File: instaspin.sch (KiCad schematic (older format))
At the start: 9 parts, among them J1 CONN_01X08, J2 CONN_01X12, J3 TMDSCNCD28069, J4 CONN_01X03, Q1 FDG1024NZ

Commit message: progress on V2 schematic
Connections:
- net labels added: TEMP_EN, TEMP_PWM, ~IFB_A
- net labels removed: IFB_A, IFB_BUS, MOTOR_TEMP, PWR_STG_TEMP, ~FLT_OTP
- wire segments 84 -> 81
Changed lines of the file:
@@
 VFB_BUS
 Text HLabel 5000 2450 2    60   Input ~ 0
-IFB_A
+~IFB_A
 Text HLabel 5000 2650 2    60   Input ~ 0
 IFB_B
 Text HLabel 5000 2850 2    60   Input ~ 0
 IFB_C
-Text HLabel 2400 1650 0    60   Input ~ 0
-PWR_STG_TEMP
-Text HLabel 2400 1850 0    60   Input ~ 0
-MOTOR_TEMP
-Text HLabel 5000 3050 2    60   Input ~ 0
-IFB_BUS
+Text HLabel 7000 1500 0    60   Input ~ 0
+TEMP_PWM
+Text HLabel 7000 1700 0    60   Output ~ 0
+TEMP_EN
 Text HLabel 2700 3250 0    60   Output ~ 0
 PWM_AH
@@
 Text HLabel 4950 4050 2    60   Input ~ 0
 ~FLT_DESAT
-Text HLabel 2550 4050 0    60   Input ~ 0
-~FLT_OTP
 Text HLabel 4950 4250 2    60   Input ~ 0
 PWR_RDY
@@
 	1950 2250 2700 2250
 Wire Wire Line
-	2400 1850 2700 1850
-Wire Wire Line
-	2400 1650 2700 1650
-Wire Wire Line
 	2400 2650 2700 2650
 Wire Wire Line
@@
 	5000 2850 4700 2850
 Wire Wire Line
-	4700 3050 5000 3050
-Wire Wire Line
 	2400 2450 2700 2450

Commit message: more v2 progress
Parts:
- added C? (x8): 2.2uF 10V, symbol C_Small
- added C? (x6): 2.2uF 6V, symbol C_Small
- added C? (x2): ? pF, symbol C_Small
- added C?: 0.1 uF, symbol C_Small
- added C?: 0.1uF 10V, symbol C_Small
- added P?: CONN_02X05, symbol CONN_02X05
- added P?: CONN_01X02, symbol CONN_01X02
- added R? (x4): 4.7k, symbol R_Small
- added R?: 170, symbol R_Small
- added R?: 330, symbol R_Small
- added U?: TMS320F28069M, MODULE, symbol TMS320F28069M
- added U?: ACPL-M61L, Housings_SOIC:SOIC-6_4.58x6.81mm_Pitch1.27mm, symbol ACPL-M61L
- added Y?: Crystal_Small, symbol Crystal_Small
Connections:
- net labels added: +1.8V, +3.3V, +3.3VA, +5VA, GPIO34, SYNCIO, TCK, TDI, TDO, TMS, ~DSP_RESET, ~TRST
- wire segments 81 -> 169
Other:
- note added: "Boot mode and JTAG"
- note added: "CAN"
- note added: "On transmitter, hand-pop LED resistors"
- moved on the sheet: D1, J1, J2, J3, J4, Q1A, Q1B, R1, W1, W2

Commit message: further V2 progress
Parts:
- added C? (x4): 0.1 uF, symbol C_Small
- added P?: CONN_01X03, symbol CONN_01X03
- added R? (x2): 1k, symbol R_Small
- added R?: 10k, symbol R_Small
- added R?: 33k, symbol R_Small
- added R?: 17k, symbol R_Small
- added R?: 330, symbol R_Small
- added U?: ADM3053, Housings_SOIC:SOIC-20_7.5x12.8mm_Pitch1.27mm, symbol ADM3053
- added W? (x7): TEST_1P, Measurement_Points:Measurement_Point_Round-SMD-Pad_Small, symbol TEST_1P
- R?: value 170 -> 170 0.5%
- R?: value 330 -> 330 0.5%
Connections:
- net labels added: CAN_RX, CAN_TX, LED1, LED2, SW_BRAKE, SW_EMERG, SW_FLIGHT, THRUST_PWM
- wire segments 169 -> 175
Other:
- note added: "Perhaps use resonator\nor SiTime?"
- moved on the sheet: J1

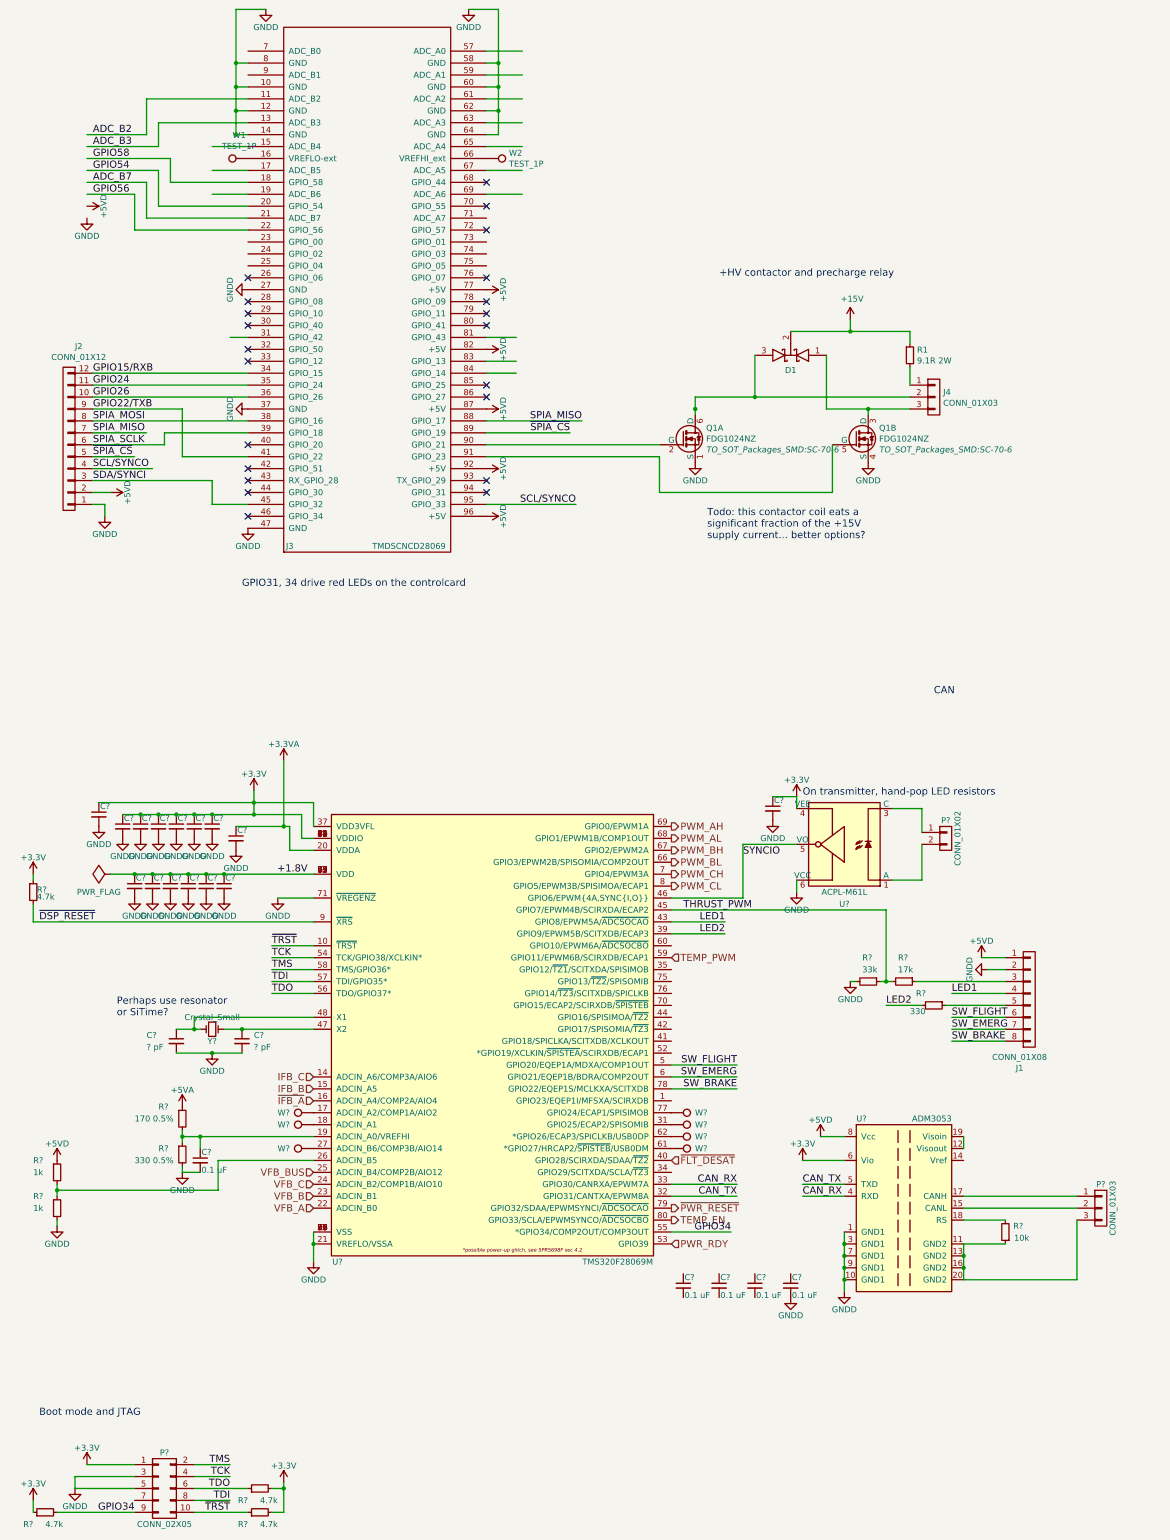
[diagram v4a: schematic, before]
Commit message: V2 schem complete, footprints not assigned
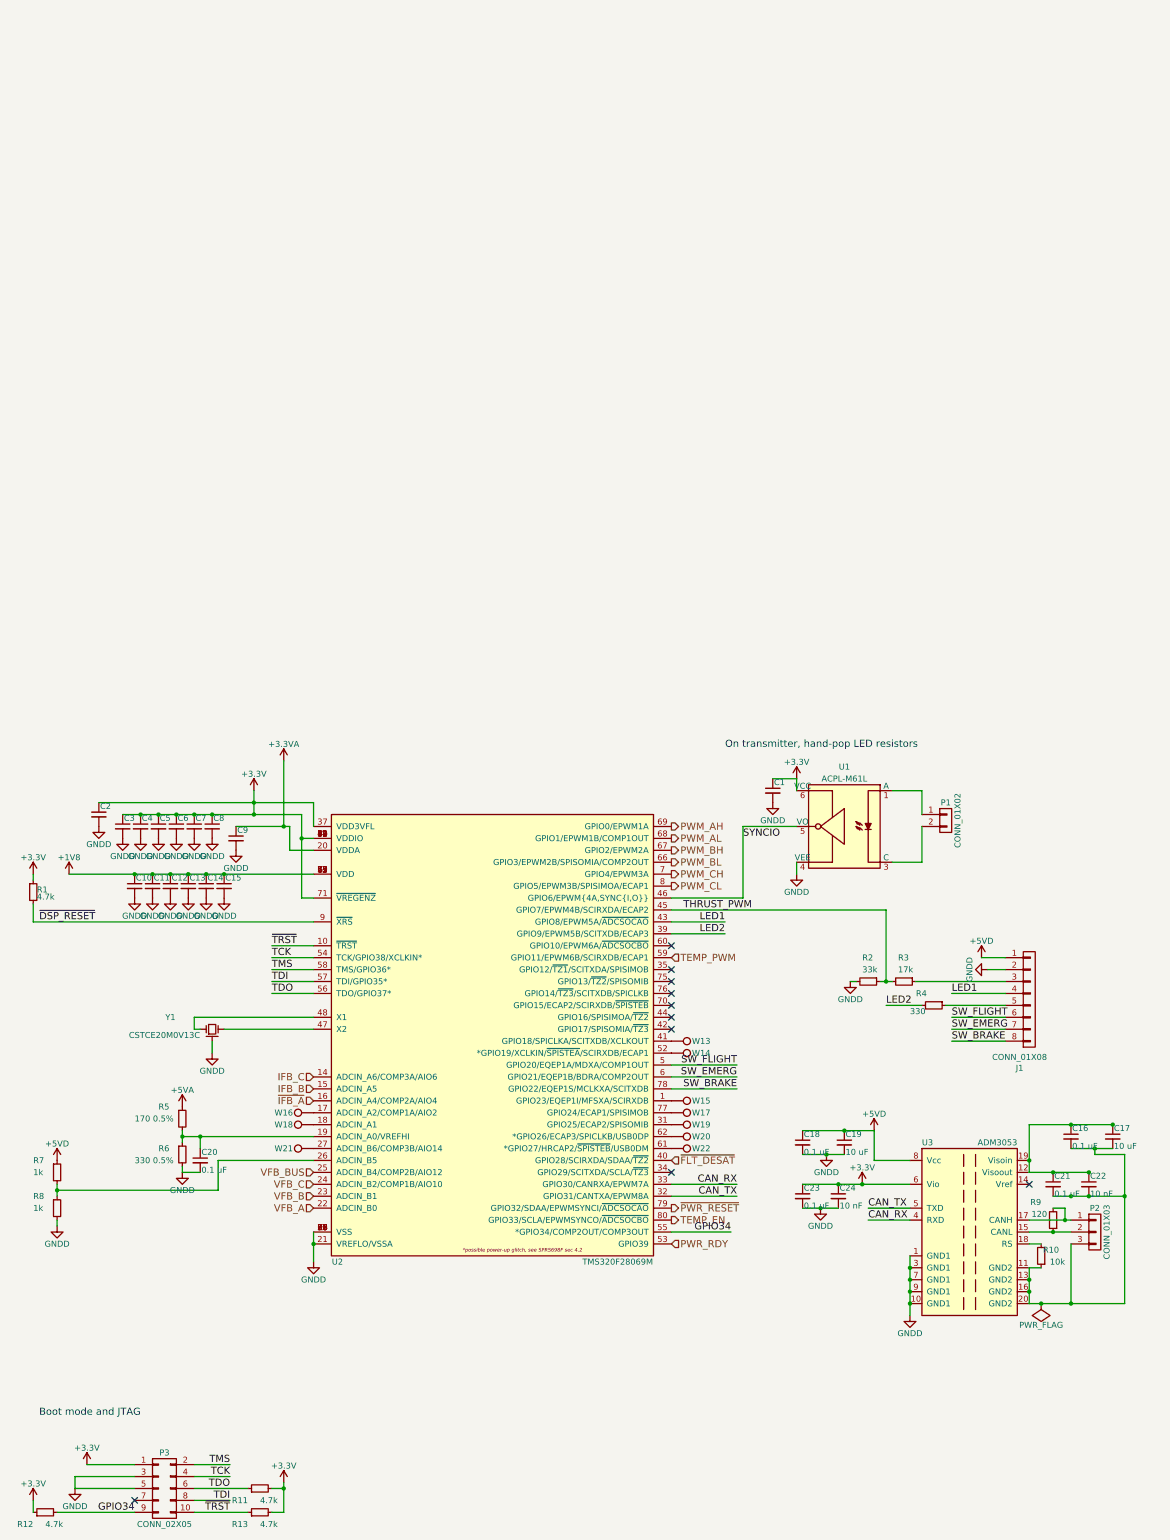
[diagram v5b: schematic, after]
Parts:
- removed C? (x2): ? pF, symbol C_Small
- removed D1: D_Schottky_x2_KCom_AKA, TO_SOT_Packages_SMD:SOT-323, symbol D_Schottky_x2_KCom_AKA
- removed J2: CONN_01X12, Connectors_Molex:Connector_Molex_PicoBlade_53261-1271, symbol CONN_01X12
- removed J3: TMDSCNCD28069, sictroller:5390213-1, symbol TMDSCNCD28069
- removed J4: CONN_01X03, sictroller:Molex-SL-3POS-RA, symbol CONN_01X03
- removed Q1: FDG1024NZ, TO_SOT_Packages_SMD:SC-70-6, symbol FDG1024NZ
- removed R1: 9.1R 2W, Resistors_ThroughHole:Resistor_Horizontal_RM15mm, symbol R_Small
- removed W1, W2: TEST_1P, Measurement_Points:Measurement_Point_Round-SMD-Pad_Small, symbol TEST_1P
- removed Y?: Crystal_Small, symbol Crystal_Small
- added C16, C21: 0.1 uF, symbol C_Small
- added C17: 10 uF, symbol C_Small
- added C22: 10 nF, symbol C_Small
- added R9: 120, symbol R_Small
- added W13, W14, W15: TEST_1P, Measurement_Points:Measurement_Point_Round-SMD-Pad_Small, symbol TEST_1P
- added Y1: CSTCE20M0V13C, symbol Ceramic_Resonator
- C19: renamed from C?; value 0.1 uF -> 10 uF
- C24: renamed from C?; value 0.1 uF -> 10 nF
- gave numbers to parts that had none: 43
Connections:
- net labels added: +1V8
- net labels removed: +1.8V, +15V, ADC_B2, ADC_B3, ADC_B7, GPIO15/RXB, GPIO22/TXB, GPIO24, GPIO26, GPIO54, GPIO56, GPIO58, SCL/SYNCO, SDA/SYNCI, SPIA_MISO, SPIA_MOSI, SPIA_SCLK, ~SPIA_CS
- wire segments 175 -> 107
- no-connect marks 22 -> 10
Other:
- note removed: "+HV contactor and precharge relay"
- note removed: "CAN"
- note removed: "GPIO31, 34 drive red LEDs on the controlcard"
- note removed: "Perhaps use resonator\nor SiTime?"
- note removed: "Todo: this contactor coil eats a\nsignificant fraction of the +15V\nsupply current... better options?"
- moved on the sheet: C1, C18, C19, C23, C24, P1, P2, R10, U1, U3

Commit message: Add TVS protection to signal I/O.  Reannotate. Assign some footprints.
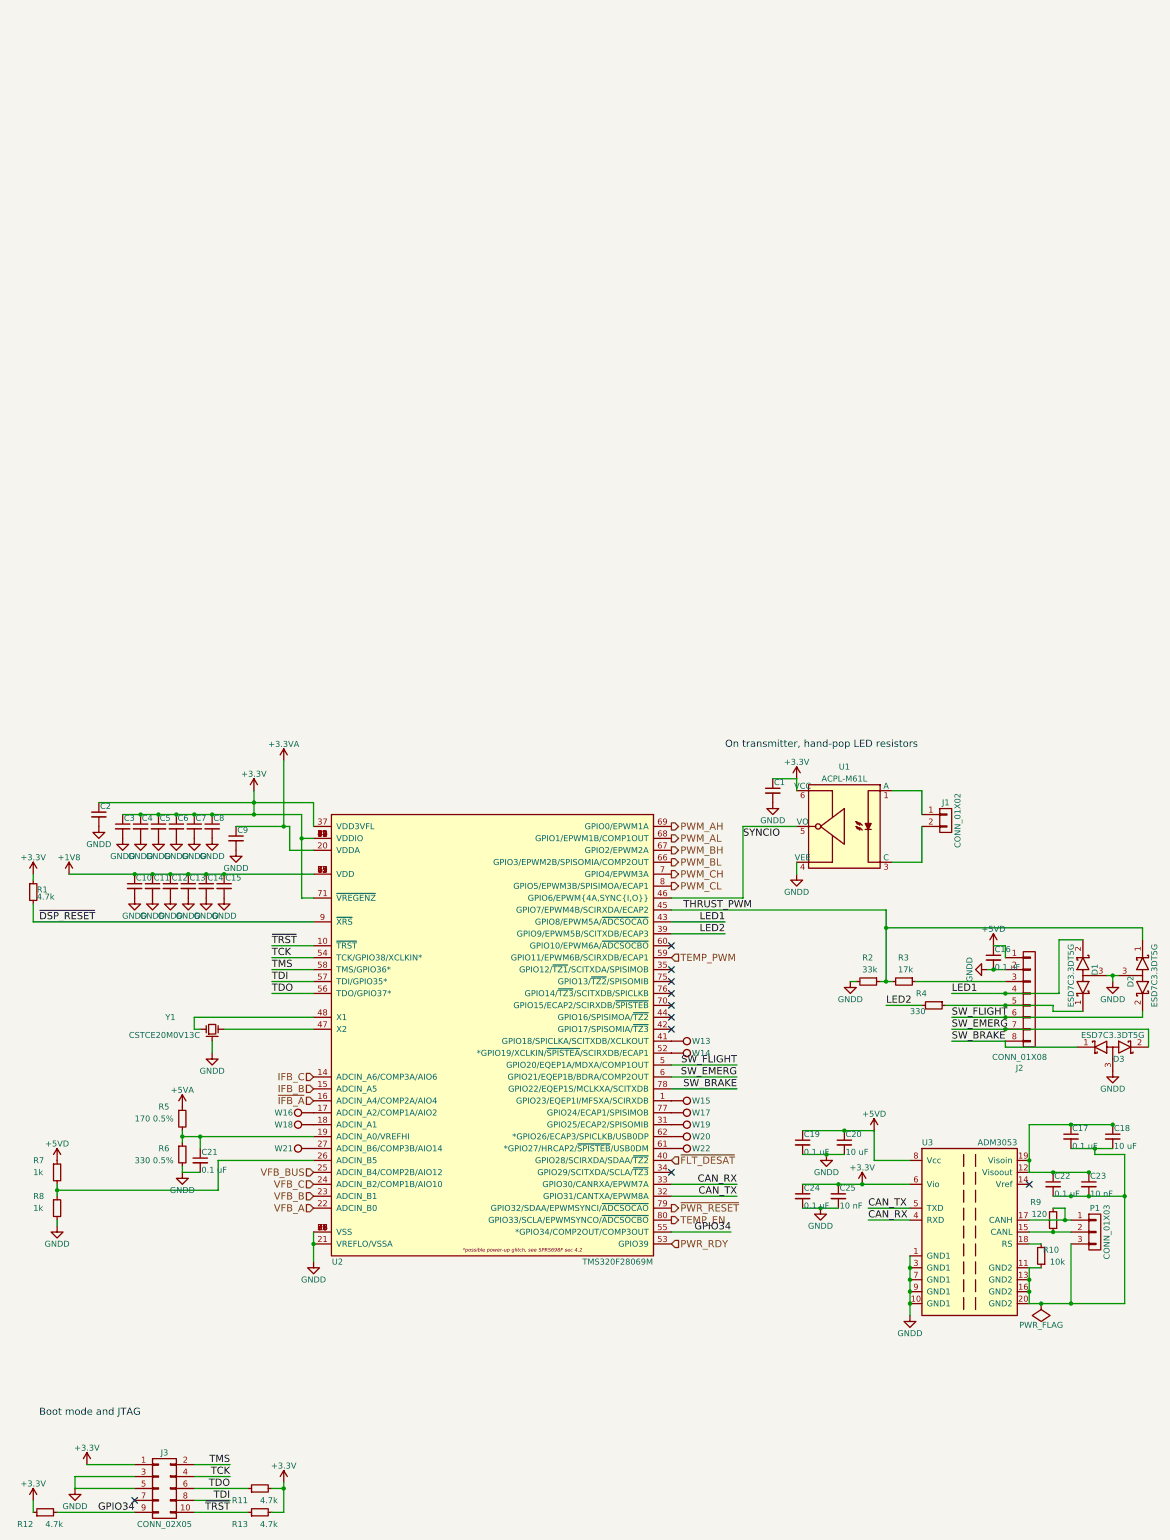
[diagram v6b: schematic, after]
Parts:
- added C16: 0.1 uF, symbol C_Small
- added D1, D2, D3: ESD7C3.3DT5G, sictroller:SOT-723, symbol D_Schottky_x2_ACom_KKA
- renumbered C16 to C17, C17 to C18, C18 to C19, C19 to C20, C20 to C21, C21 to C22, C22 to C23, C23 to C24, C24 to C25, P1 to J1, J1 to J2, P3 to J3, P2 to P1
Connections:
- net +5VD: now also C16.1
- net GNDD: now also C16.2, D1.3 (A), D2.3 (A), D3.3 (A)
- net LED1: now also D1.2 (K)
- net SW_BRAKE: now also D3.1 (K)
- net SW_EMERG: now also D3.2 (K)
- net SW_FLIGHT: now also D2.2 (K)
- net THRUST_PWM: now also D2.1 (K)
- net at J2.5 (P5), R4.1: now also D1.1 (K)

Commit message: footprints assigned for instaspin and LV power
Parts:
- C1, C16, C17, C19, C21, C22, C23, C24, C25: footprint (none) -> Capacitors_SMD:C_0402
- C10, C11, C12, C13, C14, C15, C2, C3, C4, C5, C6, C7, C8, C9: footprint (none) -> Capacitors_SMD:C_0603
- C18, C20: footprint (none) -> Capacitors_SMD:C_0805
- J1: footprint (none) -> Connectors_Molex:Molex_PicoBlade_53261-0271
- J3: footprint (none) -> sictroller:FTSH-105-01-L-DV-K
- P1: footprint (none) -> Connectors_Molex:Molex_PicoBlade_53261-0371
- U1: footprint Housings_SOIC:SOIC-6_4.58x6.81mm_Pitch1.27mm -> sictroller:ACPL-M61L_SO-5
- U2: footprint MODULE -> sictroller:PFP
- Y1: footprint (none) -> sictroller:CSTCE_V13C
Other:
- note added: "5V rail monitoring"
- note added: "CAN (indirect user interface)"
- note added: "Direct user interface"
- note added: "Inter-controller PWM sync"

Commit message: Footprints assigned for all except halfbridge-driver
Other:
- note added: "On transmitter, hand-pop LED resistors and maybe TVS"
- note removed: "On transmitter, hand-pop LED resistors"
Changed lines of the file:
@@
 SYNCIO
 Text Notes 7400 2200 0    40   ~ 0
-On transmitter, hand-pop LED resistors
+On transmitter, hand-pop LED resistors and maybe TVS
 $Comp
 L TEST_1P W16
